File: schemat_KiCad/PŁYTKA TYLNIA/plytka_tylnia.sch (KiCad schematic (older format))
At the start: 44 parts, among them P1 USB_OTG, SW1 SPST

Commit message: SPI
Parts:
- added R9: 200, Resistors_SMD:R_0805_HandSoldering, symbol R
- added SHARP_RIGHT1: PIN3, symbol CONN_01X03
- added SYGNAL_LED2: LED_RED, LEDs:LED_0805, symbol LED-RESCUE-plytka_tylnia
- renumbered BOOT to BOOT0
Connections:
- net GND: now also R9.2, SHARP_RIGHT1.2 (P2)
- net SWCLK: now also BLUETOOTH1.2 (P2)
- net USART_RX: now also MIKROPROCEK1.38 (I2S1_WS/SPI1_NSS/TIM2_CH1/TIM2_ETR/USART2_RX/PA15); no longer MIKROPROCEK1.42 (PB6/I2C1_SCL/TIM16_CH1N/TSC_G5_IO3/USART1_TX)
- net VCC_SHARP: now also SHARP_RIGHT1.3 (P3)
- net at MIKROPROCEK1.25 (PB12/SPI2_NSS/TIM1_BKIN/TSC_G6_IO2): now also SYGNAL_LED2.2 (A)
- net at MIKROPROCEK1.26 (PB13/SPI2_SCK/TIM1_CH1N/TSC_G6_IO3): now also SYGNAL_LED1.2 (A)
- net at MIKROPROCEK1.33 (COMP2_OUT/TIM1_ETR/TSC_G4_IO4/USART1_DE/USART1_RTS/PA12): now also BUTTON1.2, R4.2
- net SPI1_CLK: now reaches MIKROPROCEK1.39 (PB3/I2S1_CK/SPI1_SCK/TIM2_CH2/TSC_G5_IO1)
- net SPI1_MISO: now reaches MIKROPROCEK1.40 (PB4/I2S1_MCK/SPI1_MISO/TIM3_CH1/TSC_G5_IO2)
- net at MIKROPROCEK1.45 (PB8/CEC/I2C1_SCL/TIM16_CH1/TSC_SYNC): no longer SYGNAL_LED1.2 (A)
- net SHARP_RIGHT: now reaches MIKROPROCEK1.46 (PB9/DAC1_EXTI9/I2C1_SDA/IR_OUT/TIM17_CH1)
- net SHARP_RIGHT: now also SHARP_RIGHT1.1 (P1)
- net USART_TX renamed SPI1_SS2
- net SPI1_SS2: no longer BLUETOOTH1.2 (P2)
- new net: R9.1, SYGNAL_LED2.1 (K)
- new net SPI1_MOSI: MIKROPROCEK1.41 (PB5/I2C1_SMBA/I2S1_SD/SPI1_MOSI/TIM16_BKIN/TIM3_CH2)
- new net SPI1_SS1: MIKROPROCEK1.42 (PB6/I2C1_SCL/TIM16_CH1N/TSC_G5_IO3/USART1_TX)
- no-connect marks 14 -> 9
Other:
- moved on the sheet: BLUETOOTH1, BUTTON1, P1, R3, R4, R5, SHARP1, START_BUTTON1, SYGNAL_LED1

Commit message: bez enkoderow
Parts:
- added C?: CP1, symbol CP1
- added R?: R, symbol R
- added U?: ICL7667, symbol ICL7667
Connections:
- wire segments 122 -> 131
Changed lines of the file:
@@
 Wire Wire Line
 	1800 4700 2600 4700
+$Comp
+L ICL7667 U?
+U 1 1 58DCD442
+P 9950 9200
+F 0 "U?" H 9890 9615 50  0000 R CNN
+F 1 "ICL7667" H 9890 9540 50  0000 R CNN
+F 2 "" H 10100 8350 50  0001 L CNN
+F 3 "" H 10150 8900 50  0001 C CNN
+	1    9950 9200
+	1    0    0    -1
+$EndComp
+Wire Wire Line
+	9650 9300 9500 9300
+Wire Wire Line
+	9500 9300 9500 9650
+Wire Wire Line
+	9500 9650 10900 9650
+Wire Wire Line
+	10900 9650 10900 9300
+$Comp
+L R R?
+U 1 1 58DCE650
+P 10600 9300
+F 0 "R?" V 10680 9300 50  0000 C CNN
+F 1 "R" V 10600 9300 50  0000 C CNN
+F 2 "" V 10530 9300 50  0001 C CNN
+F 3 "" H 10600 9300 50  0001 C CNN
+	1    10600 9300
+	0    1    1    0
+$EndComp
+$Comp
+L CP1 C?
+U 1 1 58DCE6D3
+P 10400 8850
+F 0 "C?" H 10425 8950 50  0000 L CNN
+F 1 "CP1" H 10425 8750 50  0000 L CNN
+F 2 "" H 10400 8850 50  0001 C CNN
+F 3 "" H 10400 8850 50  0001 C CNN
+	1    10400 8850
+	1    0    0    -1
+$EndComp
+Wire Wire Line
+	9950 8800 9950 8650
+Wire Wire Line
+	9950 8650 10400 8650
+Wire Wire Line
+	10400 8650 10400 8700
+Wire Wire Line
+	10400 9000 10400 9650
+Connection ~ 10400 9650
+Wire Wire Line
+	10250 9300 10450 9300
 $EndSCHEMATC

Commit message: turbina
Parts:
- removed C?: CP1, symbol CP1
- removed R?: R, symbol R
- removed U?: ICL7667, symbol ICL7667
- added TURBINA1: PIN3, symbol CONN_01X03
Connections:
- net labels added: PWM_TURBINA
- wire segments 131 -> 122
- no-connect marks 9 -> 8
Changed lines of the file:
@@
 $EndComp
 $Comp
-L VCC #PWR01
+L VCC #PWR17
 U 1 1 5824A62D
 P 5800 1200
-F 0 "#PWR01" H 5800 1050 50  0001 C CNN
+F 0 "#PWR17" H 5800 1050 50  0001 C CNN
 F 1 "VCC" H 5800 1350 50  0000 C CNN
 F 2 "" H 5800 1200 50  0000 C CNN
@@
 $EndComp
 $Comp
-L GND #PWR02
+L GND #PWR19
 U 1 1 582497CD
 P 6300 2300
-F 0 "#PWR02" H 6300 2050 50  0001 C CNN
+F 0 "#PWR19" H 6300 2050 50  0001 C CNN
 F 1 "GND" H 6300 2150 50  0000 C CNN
 F 2 "" H 6300 2300 50  0000 C CNN
@@
 $EndComp
 $Comp
-L GND #PWR03
+L GND #PWR18
 U 1 1 5824B1E5
 P 6000 6700
-F 0 "#PWR03" H 6000 6450 50  0001 C CNN
+F 0 "#PWR18" H 6000 6450 50  0001 C CNN
 F 1 "GND" H 6000 6550 50  0000 C CNN
 F 2 "" H 6000 6700 50  0000 C CNN
@@
 $EndComp
 $Comp
-L VCC #PWR04
+L VCC #PWR26
 U 1 1 5825C4E2
 P 12400 1850
-F 0 "#PWR04" H 12400 1700 50  0001 C CNN
+F 0 "#PWR26" H 12400 1700 50  0001 C CNN
 F 1 "VCC" H 12400 2000 50  0000 C CNN
 F 2 "" H 12400 1850 50  0000 C CNN
@@
 L_PWM
 $Comp
-L GND #PWR05
+L GND #PWR29
 U 1 1 5825D2CD
 P 13050 3800
-F 0 "#PWR05" H 13050 3550 50  0001 C CNN
+F 0 "#PWR29" H 13050 3550 50  0001 C CNN
 F 1 "GND" H 13050 3650 50  0000 C CNN
 F 2 "" H 13050 3800 50  0000 C CNN
@@
 $EndComp
 $Comp
-L GND #PWR06
+L GND #PWR28
 U 1 1 58260AEA
 P 13050 1600
-F 0 "#PWR06" H 13050 1350 50  0001 C CNN
+F 0 "#PWR28" H 13050 1350 50  0001 C CNN
 F 1 "GND" H 13050 1450 50  0000 C CNN
 F 2 "" H 13050 1600 50  0000 C CNN
@@
 R_PWM
 $Comp
-L VCC #PWR07
+L VCC #PWR12
 U 1 1 5825FE4C
 P 3350 8350
-F 0 "#PWR07" H 3350 8200 50  0001 C CNN
+F 0 "#PWR12" H 3350 8200 50  0001 C CNN
 F 1 "VCC" H 3350 8500 50  0000 C CNN
 F 2 "" H 3350 8350 50  0000 C CNN
@@
 $EndComp
 $Comp
-L GND #PWR08
+L GND #PWR13
 U 1 1 5825FE80
 P 3700 8350
-F 0 "#PWR08" H 3700 8100 50  0001 C CNN
+F 0 "#PWR13" H 3700 8100 50  0001 C CNN
 F 1 "GND" H 3700 8200 50  0000 C CNN
 F 2 "" H 3700 8350 50  0000 C CNN
@@
 T8
 $Comp
-L GND #PWR09
+L GND #PWR9
 U 1 1 58260328
 P 1450 3000
-F 0 "#PWR09" H 1450 2750 50  0001 C CNN
+F 0 "#PWR9" H 1450 2750 50  0001 C CNN
 F 1 "GND" H 1450 2850 50  0000 C CNN
 F 2 "" H 1450 3000 50  0000 C CNN
@@
 $EndComp
 $Comp
-L GND #PWR010
+L GND #PWR31
 U 1 1 5826FC84
 P 13450 8100
-F 0 "#PWR010" H 13450 7850 50  0001 C CNN
+F 0 "#PWR31" H 13450 7850 50  0001 C CNN
 F 1 "GND" H 13450 7950 50  0000 C CNN
 F 2 "" H 13450 8100 50  0000 C CNN
@@
 $EndComp
 $Comp
-L VCC #PWR011
+L VCC #PWR32
 U 1 1 58279691
 P 14650 7450
-F 0 "#PWR011" H 14650 7300 50  0001 C CNN
+F 0 "#PWR32" H 14650 7300 50  0001 C CNN
 F 1 "VCC" H 14650 7600 50  0000 C CNN
 F 2 "" H 14650 7450 50  0000 C CNN
@@
 $EndComp
 $Comp
-L GND #PWR012
+L GND #PWR6
 U 1 1 5827AB38
 P 1400 3400
-F 0 "#PWR012" H 1400 3150 50  0001 C CNN
+F 0 "#PWR6" H 1400 3150 50  0001 C CNN
 F 1 "GND" H 1400 3250 50  0000 C CNN
 F 2 "" H 1400 3400 50  0000 C CNN
@@
 $EndComp
 $Comp
-L GND #PWR013
+L GND #PWR4
 U 1 1 5827AB7C
 P 1350 4000
-F 0 "#PWR013" H 1350 3750 50  0001 C CNN
+F 0 "#PWR4" H 1350 3750 50  0001 C CNN
 F 1 "GND" H 1350 3850 50  0000 C CNN
 F 2 "" H 1350 4000 50  0000 C CNN
@@
 $EndComp
 $Comp
-L VCC #PWR014
+L VCC #PWR10
 U 1 1 5829760E
 P 1500 2750
-F 0 "#PWR014" H 1500 2600 50  0001 C CNN
+F 0 "#PWR10" H 1500 2600 50  0001 C CNN
 F 1 "VCC" H 1500 2900 50  0000 C CNN
 F 2 "" H 1500 2750 50  0000 C CNN
@@
 $EndComp
 $Comp
-L GND #PWR015
+L GND #PWR24
 U 1 1 582A699F
 P 10550 5700
-F 0 "#PWR015" H 10550 5450 50  0001 C CNN
+F 0 "#PWR24" H 10550 5450 50  0001 C CNN
 F 1 "GND" H 10550 5550 50  0000 C CNN
 F 2 "" H 10550 5700 50  0000 C CNN
@@
 $EndComp
 $Comp
-L VCC #PWR016
+L VCC #PWR23
 U 1 1 582A69BD
 P 10550 5500
-F 0 "#PWR016" H 10550 5350 50  0001 C CNN
+F 0 "#PWR23" H 10550 5350 50  0001 C CNN
 F 1 "VCC" H 10550 5650 50  0000 C CNN
 F 2 "" H 10550 5500 50  0000 C CNN
@@
 $EndComp
 $Comp
-L GND #PWR017
+L GND #PWR33
 U 1 1 582C3C66
 P 14700 1600
-F 0 "#PWR017" H 14700 1350 50  0001 C CNN
+F 0 "#PWR33" H 14700 1350 50  0001 C CNN
 F 1 "GND" H 14700 1450 50  0000 C CNN
 F 2 "" H 14700 1600 50  0000 C CNN
@@
 $EndComp
 $Comp
-L GND #PWR018
+L GND #PWR8
 U 1 1 582CED00
 P 1400 5850
-F 0 "#PWR018" H 1400 5600 50  0001 C CNN
+F 0 "#PWR8" H 1400 5600 50  0001 C CNN
 F 1 "GND" H 1400 5700 50  0000 C CNN
 F 2 "" H 1400 5850 50  0000 C CNN
@@
 $EndComp
 $Comp
-L GND #PWR019
+L GND #PWR1
 U 1 1 582D02EC
 P 1200 4700
-F 0 "#PWR019" H 1200 4450 50  0001 C CNN
+F 0 "#PWR1" H 1200 4450 50  0001 C CNN
 F 1 "GND" H 1200 4550 50  0000 C CNN
 F 2 "" H 1200 4700 50  0000 C CNN
@@
 $EndComp
 $Comp
-L VCC #PWR020
+L VCC #PWR2
 U 1 1 582D030A
 P 1200 4950
-F 0 "#PWR020" H 1200 4800 50  0001 C CNN
+F 0 "#PWR2" H 1200 4800 50  0001 C CNN
 F 1 "VCC" H 1200 5100 50  0000 C CNN
 F 2 "" H 1200 4950 50  0000 C CNN
@@
 $EndComp
 $Comp
-L GND #PWR021
+L GND #PWR27
 U 1 1 5829AC4F
 P 12600 8150
-F 0 "#PWR021" H 12600 7900 50  0001 C CNN
+F 0 "#PWR27" H 12600 7900 50  0001 C CNN
 F 1 "GND" H 12600 8000 50  0000 C CNN
 F 2 "" H 12600 8150 50  0000 C CNN
@@
 NoConn ~ 2600 3400
 $Comp
-L PWR_FLAG #FLG022
+L PWR_FLAG #FLG1
 U 1 1 582A5677
 P 1400 3400
-F 0 "#FLG022" H 1400 3495 50  0001 C CNN
+F 0 "#FLG1" H 1400 3495 50  0001 C CNN
 F 1 "PWR_FLAG" H 1400 3580 50  0000 C CNN
 F 2 "" H 1400 3400 50  0000 C CNN
@@
 $EndComp
 $Comp
-L PWR_FLAG #FLG023
+L PWR_FLAG #FLG2
 U 1 1 582A5B0F
 P 6400 2500
-F 0 "#FLG023" H 6400 2595 50  0001 C CNN
+F 0 "#FLG2" H 6400 2595 50  0001 C CNN
 F 1 "PWR_FLAG" H 6400 2680 50  0000 C CNN
 F 2 "" H 6400 2500 50  0000 C CNN
@@
 USART_TX
 $Comp
-L GND #PWR024
+L GND #PWR15
 U 1 1 582E66DC
 P 5100 9150
-F 0 "#PWR024" H 5100 8900 50  0001 C CNN
+F 0 "#PWR15" H 5100 8900 50  0001 C CNN
 F 1 "GND" H 5100 9000 50  0000 C CNN
 F 2 "" H 5100 9150 50  0000 C CNN
@@
 $EndComp
 $Comp
-L VCC #PWR025
+L VCC #PWR14
 U 1 1 582E673A
 P 5000 9250
-F 0 "#PWR025" H 5000 9100 50  0001 C CNN
+F 0 "#PWR14" H 5000 9100 50  0001 C CNN
 F 1 "VCC" H 5000 9400 50  0000 C CNN
 F 2 "" H 5000 9250 50  0000 C CNN
@@
 $EndComp
 $Comp
-L GND #PWR026
+L GND #PWR16
 U 1 1 58338561
 P 5600 2300
-F 0 "#PWR026" H 5600 2050 50  0001 C CNN
+F 0 "#PWR16" H 5600 2050 50  0001 C CNN
 F 1 "GND" H 5600 2150 50  0000 C CNN
 F 2 "" H 5600 2300 50  0000 C CNN
@@
 RESET
 $Comp
-L VCC #PWR027
+L VCC #PWR3
 U 1 1 583CD7DF
 P 1300 8650
-F 0 "#PWR027" H 1300 8500 50  0001 C CNN
+F 0 "#PWR3" H 1300 8500 50  0001 C CNN
 F 1 "VCC" H 1300 8800 50  0000 C CNN
 F 2 "" H 1300 8650 50  0000 C CNN
@@
 $EndComp
 $Comp
-L GND #PWR028
+L GND #PWR5
 U 1 1 583CE05F
 P 1350 9500
-F 0 "#PWR028" H 1350 9250 50  0001 C CNN
+F 0 "#PWR5" H 1350 9250 50  0001 C CNN
 F 1 "GND" H 1350 9350 50  0000 C CNN
 F 2 "" H 1350 9500 50  0000 C CNN
@@
 $EndComp
 $Comp
-L GND #PWR029
+L GND #PWR25
 U 1 1 58DBB195
 P 10950 8150
-F 0 "#PWR029" H 10950 7900 50  0001 C CNN
+F 0 "#PWR25" H 10950 7900 50  0001 C CNN
 F 1 "GND" H 10950 8000 50  0000 C CNN
 F 2 "" H 10950 8150 50  0001 C CNN
@@
 $EndComp
 $Comp
-L GND #PWR030
+L GND #PWR30
 U 1 1 58DC29CF
 P 13450 6850
-F 0 "#PWR030" H 13450 6600 50  0001 C CNN
+F 0 "#PWR30" H 13450 6600 50  0001 C CNN
 F 1 "GND" H 13450 6700 50  0000 C CNN
 F 2 "" H 13450 6850 50  0000 C CNN
@@
 $EndComp
 $Comp
-L GND #PWR031
+L GND #PWR20
 U 1 1 58DCF56A
 P 6600 9150
-F 0 "#PWR031" H 6600 8900 50  0001 C CNN
+F 0 "#PWR20" H 6600 8900 50  0001 C CNN
 F 1 "GND" H 6600 9000 50  0000 C CNN
 F 2 "" H 6600 9150 50  0001 C CNN
@@
 $EndComp
 $Comp
-L VCC #PWR032
+L VCC #PWR11
 U 1 1 58DBFCD6
 P 2000 3200
-F 0 "#PWR032" H 2000 3050 50  0001 C CNN
+F 0 "#PWR11" H 2000 3050 50  0001 C CNN
 F 1 "VCC" H 2000 3350 50  0000 C CNN
 F 2 "" H 2000 3200 50  0001 C CNN
@@
 VCC_SHARP
 $Comp
-L GND #PWR033
+L GND #PWR21
 U 1 1 58DD50DC
 P 8000 9150
-F 0 "#PWR033" H 8000 8900 50  0001 C CNN
+F 0 "#PWR21" H 8000 8900 50  0001 C CNN
 F 1 "GND" H 8000 9000 50  0000 C CNN
 F 2 "" H 8000 9150 50  0001 C CNN
@@
 $EndComp
 $Comp
-L GND #PWR034
+L GND #PWR7
 U 1 1 58DD7D15
 P 1400 5550
-F 0 "#PWR034" H 1400 5300 50  0001 C CNN
+F 0 "#PWR7" H 1400 5300 50  0001 C CNN
 F 1 "GND" H 1400 5400 50  0000 C CNN
 F 2 "" H 1400 5550 50  0000 C CNN
@@
 	1    0    0    -1
 $EndComp
-NoConn ~ 2600 5300
 Wire Wire Line
 	3700 8450 3700 8350
@@
 Wire Wire Line
 	1800 4700 2600 4700
-$Comp
-L ICL7667 U?
-U 1 1 58DCD442
-P 9950 9200
-F 0 "U?" H 9890 9615 50  0000 R CNN
-F 1 "ICL7667" H 9890 9540 50  0000 R CNN
-F 2 "" H 10100 8350 50  0001 L CNN
-F 3 "" H 10150 8900 50  0001 C CNN
-	1    9950 9200
-	1    0    0    -1
-$EndComp
-Wire Wire Line
-	9650 9300 9500 9300
-Wire Wire Line
-	9500 9300 9500 9650
-Wire Wire Line
-	9500 9650 10900 9650
-Wire Wire Line
-	10900 9650 10900 9300
-$Comp
-L R R?
-U 1 1 58DCE650
-P 10600 9300
-F 0 "R?" V 10680 9300 50  0000 C CNN
-F 1 "R" V 10600 9300 50  0000 C CNN
-F 2 "" V 10530 9300 50  0001 C CNN
-F 3 "" H 10600 9300 50  0001 C CNN
-	1    10600 9300
-	0    1    1    0
-$EndComp
-$Comp
-L CP1 C?
-U 1 1 58DCE6D3
-P 10400 8850
-F 0 "C?" H 10425 8950 50  0000 L CNN
-F 1 "CP1" H 10425 8750 50  0000 L CNN
-F 2 "" H 10400 8850 50  0001 C CNN
-F 3 "" H 10400 8850 50  0001 C CNN
-	1    10400 8850
-	1    0    0    -1
-$EndComp
-Wire Wire Line
-	9950 8800 9950 8650
-Wire Wire Line
-	9950 8650 10400 8650
-Wire Wire Line
-	10400 8650 10400 8700
-Wire Wire Line
-	10400 9000 10400 9650
-Connection ~ 10400 9650
-Wire Wire Line
-	10250 9300 10450 9300
+Text Label 9450 9100 2    60   ~ 0
+PWM_TURBINA
+$Comp
+L CONN_01X03 TURBINA1
+U 1 1 58DDB2AB
+P 9650 9100
+F 0 "TURBINA1" H 9650 9300 50  0000 C CNN
+F 1 "PIN3" V 9750 9100 50  0000 C CNN
+F 2 "" H 9650 9100 50  0001 C CNN
+F 3 "" H 9650 9100 50  0001 C CNN
+	1    9650 9100
+	1    0    0    -1
+$EndComp
+Text Label 9450 9000 2    60   ~ 0
+BATERIA
+$Comp
+L GND #PWR22
+U 1 1 58DDDCB7
+P 9450 9200
+F 0 "#PWR22" H 9450 8950 50  0001 C CNN
+F 1 "GND" H 9450 9050 50  0000 C CNN
+F 2 "" H 9450 9200 50  0001 C CNN
+F 3 "" H 9450 9200 50  0001 C CNN
+	1    9450 9200
+	0    1    1    0
+$EndComp
 $EndSCHEMATC

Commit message: zrobiony przełącznik boot0
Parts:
- removed BOOT0: BOOT0pin, symbol SW_PUSH
- added BOOT0: SWITCH, symbol CONN_01X03
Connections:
- net GND: now also BOOT0.3 (P3)
- net VCC: now also BOOT0.1 (P1)
- net BOOT0: now reaches MIKROPROCEK1.44 (BOOT0)
- net BOOT0: now also BOOT0.2 (P2)
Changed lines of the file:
@@
 SHARP
-$Comp
-L SW_PUSH BOOT0
-U 1 1 58DBFC59
-P 2300 3200
-F 0 "BOOT0" H 2450 3310 50  0000 C CNN
-F 1 "BOOT0pin" H 2300 3120 50  0000 C CNN
-F 2 "" H 2300 3200 50  0000 C CNN
-F 3 "" H 2300 3200 50  0000 C CNN
-	1    2300 3200
-	1    0    0    -1
-$EndComp
-$Comp
-L VCC #PWR11
-U 1 1 58DBFCD6
-P 2000 3200
-F 0 "#PWR11" H 2000 3050 50  0001 C CNN
-F 1 "VCC" H 2000 3350 50  0000 C CNN
-F 2 "" H 2000 3200 50  0001 C CNN
-F 3 "" H 2000 3200 50  0001 C CNN
-	1    2000 3200
-	0    -1   -1   0
-$EndComp
 $Comp
 L STM32F051C8Tx MIKROPROCEK1
@@
 	0    1    1    0
 $EndComp
+Text Label 2600 3200 2    60   ~ 0
+BOOT0
+Text Label 10300 9100 2    60   ~ 0
+BOOT0
+$Comp
+L VCC #PWR?
+U 1 1 58E56396
+P 10300 9000
+F 0 "#PWR?" H 10300 8850 50  0001 C CNN
+F 1 "VCC" H 10300 9150 50  0000 C CNN
+F 2 "" H 10300 9000 50  0001 C CNN
+F 3 "" H 10300 9000 50  0001 C CNN
+	1    10300 9000
+	1    0    0    -1
+$EndComp
+$Comp
+L CONN_01X03 BOOT0
+U 1 1 58E56485
+P 10500 9100
+F 0 "BOOT0" H 10500 9300 50  0000 C CNN
+F 1 "SWITCH" V 10600 9100 50  0000 C CNN
+F 2 "" H 10500 9100 50  0001 C CNN
+F 3 "" H 10500 9100 50  0001 C CNN
+	1    10500 9100
+	1    0    0    -1
+$EndComp
+$Comp
+L GND #PWR?
+U 1 1 58E56822
+P 10300 9200
+F 0 "#PWR?" H 10300 8950 50  0001 C CNN
+F 1 "GND" H 10300 9050 50  0000 C CNN
+F 2 "" H 10300 9200 50  0001 C CNN
+F 3 "" H 10300 9200 50  0001 C CNN
+	1    10300 9200
+	1    0    0    -1
+$EndComp
 $EndSCHEMATC

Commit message: PCB-enkodery
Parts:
- added LED_RGB1: LED_CRGB, warsztaty:LED_RGB_0805, symbol LED_CRGB
- added R10, R11, R12, R13: R, Resistors_SMD:R_0805_HandSoldering, symbol R
- BATERIA1: footprint warsztatymisc:zl_zasilania -> Pin_Headers:Pin_Header_Straight_1x02_Pitch2.00mm
- BLUETOOTH1: footprint warsztatymisc:pin_array_4x1 -> Pin_Headers:Pin_Header_Straight_1x04_Pitch2.00mm
- BOOT0, SHARP1, SHARP_RIGHT1, TURBINA1: footprint (none) -> Pin_Headers:Pin_Header_Straight_1x03_Pitch2.00mm
- Bezpiecznik1: footprint (none) -> Fuse_Holders_and_Fuses:Fuse_SMD1206_HandSoldering
- MOTOR_L2, MOTOR_R1: footprint warsztatymisc:silnik -> Pin_Headers:Pin_Header_Straight_1x02_Pitch2.00mm
- P1: footprint warsztatymisc:USB-MINI-B-SMD -> Connectors_USB:USB_Micro-B_Molex-105017-0001
- R7, R8: footprint (none) -> Resistors_SMD:R_0805_HandSoldering
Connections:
- net GND: now also R10.2
- net LED_R: now reaches MIKROPROCEK1.2 (PC13/RTC_OUT_ALARM/RTC_OUT_CALIB/RTC_TAMP1/RTC_TS/SYS_WKUP2)
- net LED_R: now also R11.1
- net LED_G: now reaches MIKROPROCEK1.3 (PC14/RCC_OSC32_IN)
- net LED_G: now also R12.1
- net LED_B: now reaches MIKROPROCEK1.4 (PC15/RCC_OSC32_OUT)
- net LED_B: now also R13.1
- new net: LED_RGB1.1 (K), R10.1
- new net: LED_RGB1.2 (RA), R11.2
- new net: LED_RGB1.3 (GA), R12.2
- new net: LED_RGB1.4 (BA), R13.2
- no-connect marks 8 -> 5

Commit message: tył do druku
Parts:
- removed BUTTON1: PUSH, warsztatymisc:SW_06_SMD, symbol SW_PUSH
- removed R4: 10k, Resistors_SMD:R_0805_HandSoldering, symbol R
- removed R5, R9: 200, Resistors_SMD:R_0805_HandSoldering, symbol R
- removed SYGNAL_LED1: LED_BLUE, LEDs:LED_0805, symbol LED-RESCUE-plytka_tylnia
- removed SYGNAL_LED2: LED_RED, LEDs:LED_0805, symbol LED-RESCUE-plytka_tylnia
- added C1: 4,7uF, Capacitors_SMD:C_0805_HandSoldering, symbol CP
- added C12: 100nF, Capacitors_SMD:C_0805_HandSoldering, symbol C
- added C17: C, Capacitors_SMD:C_0805_HandSoldering, symbol C
- added J1: CONN_01X04, Pin_Headers:Pin_Header_Straight_1x04_Pitch2.00mm, symbol CONN_01X04
- added J2, J3: PIN8, Pin_Headers:Pin_Header_Straight_1x08_Pitch2.00mm, symbol CONN_01X08
- added SWITCH1: Przełącznik_dźwigniowy_podwójny_On-On_MTS, warsztaty:PRZEŁĄCZNIK_2x3, symbol Przełącznik_dźwigniowy_podwójny_On-On_MTS
- BATERIA1: footprint Pin_Headers:Pin_Header_Straight_1x02_Pitch2.00mm -> misc:zl_zasilania
- BOOT0: footprint Pin_Headers:Pin_Header_Straight_1x03_Pitch2.00mm -> warsztaty:PRZEŁĄCZNIK_1x3
- MIKROPROCEK1: footprint warsztatymisc:LQFP48 -> misc:LQFP48
- PRZYCISK_RESET1, START_BUTTON1: footprint warsztatymisc:SW_06_SMD -> misc:SW_06_SMD
- REZONATOR1: footprint warsztatymisc:Kwarc_SMD_Mini -> misc:Kwarc_SMD_Mini
- TRANSISTOR1: footprint Power_Integrations:TO-220 -> misc:SOT23-3
- WYJSCIE_DO_PLYTKI_PRZEDNIEJ1: footprint warsztatymisc:fpc_10_pin -> misc:fpc_10_pin
- Włącznik1: renamed from SW1; value SPST -> switch; footprint warsztatymisc:tact_switch_smd -> warsztaty:PRZEŁĄCZNIK_1x2
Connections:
- net PWM_TURBINA is gone; now on net TURBINA_PWM: TURBINA1.2 (P2)
- net GND: now also C1.2, C12.2, C17.2, J1.4 (P4), J2.8 (P8), J3.8 (P8)
- net LIPOL_POMIAR: now also C17.1
- net SPI1_CLK: now also J2.5 (P5), J3.5 (P5)
- net SPI1_MISO: now also J2.7 (P7), J3.7 (P7)
- net SPI1_MOSI: now also J2.6 (P6), J3.6 (P6)
- net SPI1_SS1: now also J2.4 (P4)
- net SPI1_SS2: now also J3.4 (P4)
- net T1: now also WYJSCIE_DO_PLYTKI_PRZEDNIEJ1.1 (P1); no longer WYJSCIE_DO_PLYTKI_PRZEDNIEJ1.8 (P8)
- net T2: now also WYJSCIE_DO_PLYTKI_PRZEDNIEJ1.2 (P2); no longer WYJSCIE_DO_PLYTKI_PRZEDNIEJ1.7 (P7)
- net T3: now also WYJSCIE_DO_PLYTKI_PRZEDNIEJ1.3 (P3); no longer WYJSCIE_DO_PLYTKI_PRZEDNIEJ1.6 (P6)
- net T4: now also WYJSCIE_DO_PLYTKI_PRZEDNIEJ1.4 (P4); no longer WYJSCIE_DO_PLYTKI_PRZEDNIEJ1.5 (P5)
- net T5: now also WYJSCIE_DO_PLYTKI_PRZEDNIEJ1.5 (P5); no longer WYJSCIE_DO_PLYTKI_PRZEDNIEJ1.4 (P4)
- net T6: now also WYJSCIE_DO_PLYTKI_PRZEDNIEJ1.6 (P6); no longer WYJSCIE_DO_PLYTKI_PRZEDNIEJ1.3 (P3)
- net T7: now also WYJSCIE_DO_PLYTKI_PRZEDNIEJ1.7 (P7); no longer WYJSCIE_DO_PLYTKI_PRZEDNIEJ1.2 (P2)
- net T8: now also WYJSCIE_DO_PLYTKI_PRZEDNIEJ1.8 (P8); no longer WYJSCIE_DO_PLYTKI_PRZEDNIEJ1.1 (P1)
- net VCC: now also C1.1, C12.1, J2.2 (P2), J3.2 (P2)
- net at R3.2, START_BUTTON1.2: now also MIKROPROCEK1.33 (COMP2_OUT/TIM1_ETR/TSC_G4_IO4/USART1_DE/USART1_RTS/PA12); no longer MIKROPROCEK1.20 (PB2/TSC_G3_IO4)
- net TURBINA_PWM: now reaches MIKROPROCEK1.21 (PB10/CEC/I2C2_SCL/TIM2_CH3/TSC_SYNC)
- net at C2.1, REZONATOR1.2: now also SWITCH1.3; no longer MIKROPROCEK1.5 (PF0/RCC_OSC_IN)
- net at C3.1, REZONATOR1.1: now also SWITCH1.6; no longer MIKROPROCEK1.6 (PF1/RCC_OSC_OUT)
- net SHARP renamed SHARP_LEFT
- net VCC_SHARP renamed 5V
- net 5V: now also J1.1 (P1), J2.1 (P1), J3.1 (P1)
- new net ECHO: J1.3 (P3), SWITCH1.4 (5)
- new net OSC_IN: MIKROPROCEK1.5 (PF0/RCC_OSC_IN), SWITCH1.2
- new net OSC_OUT: MIKROPROCEK1.6 (PF1/RCC_OSC_OUT), SWITCH1.4 (5)
- new net TRIG: J1.2 (P2), SWITCH1.1
- no-connect marks 5 -> 10
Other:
- moved on the sheet: BATERIA1, BLUETOOTH1, BOOT0, Bezpiecznik1, C10, C11, C13, C14, C15, C16, C2, C3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

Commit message: poprawiony echo/trig
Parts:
- removed SWITCH1: Przełącznik_dźwigniowy_podwójny_On-On_MTS, warsztaty:PRZEŁĄCZNIK_2x3, symbol Przełącznik_dźwigniowy_podwójny_On-On_MTS
- added R14, R15, R4, R5, R9: R, Resistors_SMD:R_0805_HandSoldering, symbol R
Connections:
- net OSC_IN is gone; now on an unnamed net: MIKROPROCEK1.5 (PF0/RCC_OSC_IN)
- net OSC_OUT is gone; now on an unnamed net: MIKROPROCEK1.6 (PF1/RCC_OSC_OUT)
- net ECHO: now also R14.1
- net GND: now also R13.1, R15.2, R4.1, R5.1
- net LED_B: now also R9.1; no longer R13.1
- net TRIG: now also MIKROPROCEK1.36 (PF7/I2C2_SDA)
- net at MIKROPROCEK1.35 (PF6/I2C2_SCL): now also R14.2, R15.1
- net at LED_RGB1.2 (RA), R11.2: now also R4.2
- net at LED_RGB1.3 (GA), R12.2: now also R5.2
- net at LED_RGB1.4 (BA), R13.2: now also R9.2
- no-connect marks 10 -> 8
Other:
- moved on the sheet: C2, C3, R11, R12, R13, REZONATOR1

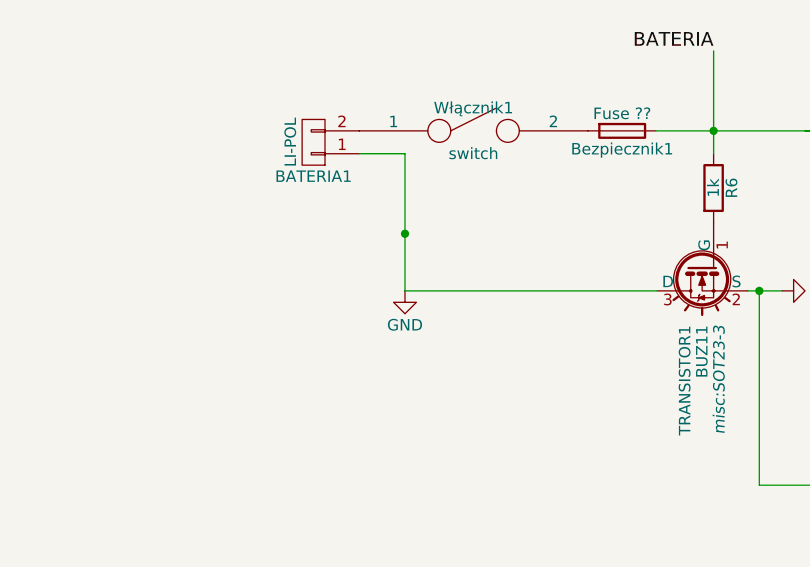
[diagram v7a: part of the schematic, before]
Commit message: zabezpieczenie przed odwrotną polaryzacją, ścieżki spi 0.6 , zwykle 0.4 zasilanie 1
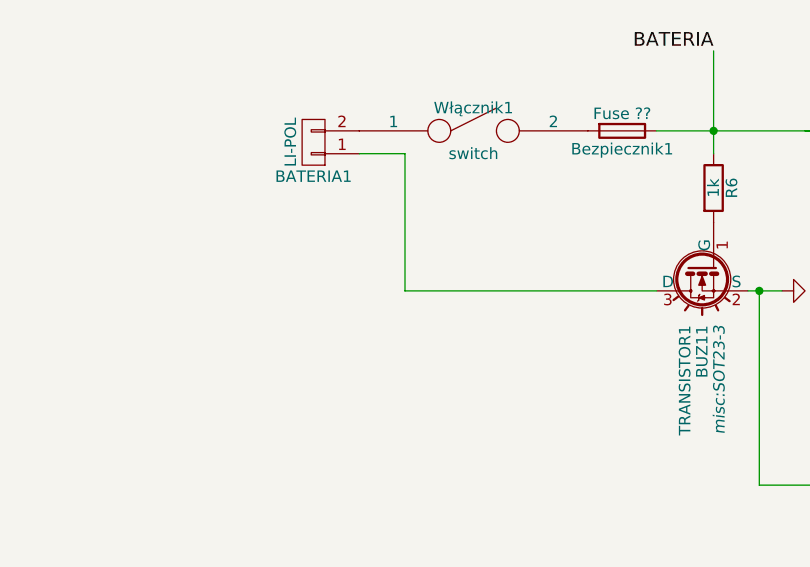
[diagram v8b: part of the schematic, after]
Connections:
- net GND: no longer BATERIA1.1 (P1), TRANSISTOR1.3 (D)
- new net: BATERIA1.1 (P1), TRANSISTOR1.3 (D)
